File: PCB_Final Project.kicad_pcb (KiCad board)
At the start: 2 copper layers, 29 parts, among them J1 Conn_01x02_Socket, J2 Conn_01x02_Pin, J3 Conn_01x02_Socket, K1 Relay_SPDT, K2 Relay_SPDT, Q1 NPN, Q2 NPN, U1 WeMos_D1_mini, U2 PC817, U3 PC817

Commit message: small correction on pcb
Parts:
- moved REF** 10.8 mm to (134.6, 53.3)
- moved REF** 7.62 mm to (134.6, 121.9)
- moved REF** 7.62 mm to (33.0, 53.3)
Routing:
- net GND: track 270.7 -> 290.9 mm
- net Net-(D4-A): track 16.4 -> 13.6 mm
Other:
- board outline added: 114.3 x 81.3 mm
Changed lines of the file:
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@@
     (property "ki_keywords" "Single Pole Relay SPDT")
     (attr through_hole)
-    (fp_text reference "K1" (at 8.1 9.2) (layer "F.SilkS")
-        (effects (font (size 1 1) (thickness 0.15)))
-    )
-    (fp_text value "Relay_SPDT" (at 8 -9.6) (layer "F.Fab")
+    (fp_text reference "K1" (at 8.8152 -9.0368) (layer "F.SilkS")
+        (effects (font (size 1 1) (thickness 0.15)))
+    )
+    (fp_text value "Relay_SPDT" (at 8.3072 0.1072) (layer "F.Fab")
         (effects (font (size 1 1) (thickness 0.15)))
     )
@@
     (property "ki_keywords" "cap capacitor")
     (attr smd)
-    (fp_text reference "C1" (at 0 -1.68) (layer "F.SilkS")
+    (fp_text reference "C1" (at 0 1.778) (layer "F.SilkS")
         (effects (font (size 1 1) (thickness 0.15)))
     )
@@
     (property "ki_keywords" "R res resistor")
     (attr smd)
-    (fp_text reference "R3" (at 0 -1.65) (layer "F.SilkS")
+    (fp_text reference "R3" (at 0.6115 1.778) (layer "F.SilkS")
         (effects (font (size 1 1) (thickness 0.15)))
     )
@@
   )
   (footprint "MountingHole:MountingHole_3.2mm_M3" (layer "F.Cu")
-    (at 127 60.96)
+    (at 134.62 53.34)
     (descr "Mounting Hole 3.2mm, no annular, M3")
     (tags "mounting hole 3.2mm no annular m3")
@@
     (property "ki_keywords" "R res resistor")
     (attr smd)
-    (fp_text reference "R2" (at 0 -21.2598) (layer "F.SilkS")
+    (fp_text reference "R2" (at 0.0235 -1.7018) (layer "F.SilkS")
         (effects (font (size 1 1) (thickness 0.15)))
     )
@@
     (property "ki_keywords" "DHT22, temperature, humidity")
     (attr through_hole)
-    (fp_text reference "TH1" (at 0 7.35) (layer "F.SilkS")
+    (fp_text reference "TH1" (at 1.016 -4.318) (layer "F.SilkS")
         (effects (font (size 1 1) (thickness 0.15)))
     )
@@
     (property "ki_keywords" "connector")
     (attr exclude_from_pos_files)
-    (fp_text reference "J1" (at 4.4 -3.4 90) (layer "F.SilkS")
+    (fp_text reference "J1" (at 12.9286 0) (layer "F.SilkS")
         (effects (font (size 1 1) (thickness 0.15)))
     )
@@
     (property "ki_keywords" "LED diode")
     (attr smd)
-    (fp_text reference "POWER1" (at 0 -4.064) (layer "F.SilkS")
+    (fp_text reference "POWER1" (at 0 -1.778) (layer "F.SilkS")
         (effects (font (size 1 1) (thickness 0.15)))
     )
@@
   )
   (footprint "MountingHole:MountingHole_3.2mm_M3" (layer "F.Cu")
-    (at 33.02 60.96)
+    (at 33.02 53.34)
     (descr "Mounting Hole 3.2mm, no annular, M3")
     (tags "mounting hole 3.2mm no annular m3")
@@
   )
   (footprint "MountingHole:MountingHole_3.2mm_M3" (layer "F.Cu")
-    (at 127 121.92)
+    (at 134.62 121.92)
     (descr "Mounting Hole 3.2mm, no annular, M3")
     (tags "mounting hole 3.2mm no annular m3")
@@
     (property "ki_keywords" "connector")
     (attr exclude_from_pos_files)
-    (fp_text reference "J3" (at 4.4 -3.4 90) (layer "F.SilkS")
+    (fp_text reference "J3" (at 12.8016 -0.0508) (layer "F.SilkS")
         (effects (font (size 1 1) (thickness 0.15)))
     )
@@
     (property "ki_keywords" "LED diode")
     (attr smd)
-    (fp_text reference "D2" (at 0 -3.7846) (layer "F.SilkS")
+    (fp_text reference "D2" (at 1.1915 -1.7526) (layer "F.SilkS")
         (effects (font (size 1 1) (thickness 0.15)))
     )
@@
     (property "ki_keywords" "simulation")
     (attr smd)
-    (fp_text reference "Q1" (at 0 -2.45) (layer "F.SilkS")
+    (fp_text reference "Q1" (at 0 2.6924) (layer "F.SilkS")
         (effects (font (size 1 1) (thickness 0.15)))
     )
@@
     (property "ki_keywords" "NPN DC Optocoupler")
     (attr smd)
-    (fp_text reference "U3" (at 0 -3.6) (layer "F.SilkS")
+    (fp_text reference "U3" (at -1.0922 -3.556) (layer "F.SilkS")
         (effects (font (size 1 1) (thickness 0.15)))
     )
@@
     )
   )
+  (gr_rect (start 25.4 48.26) (end 139.7 129.54)
+    (stroke (width 0.1) (type default)) (fill none) (layer "Edge.Cuts"))
   (segment (start 64.77 87.63) (end 64.77 93.206) (width 0.33) (layer "F.Cu") (net 1))
   (segment (start 62.23 87.63) (end 62.23 93.206) (width 0.33) (layer "F.Cu") (net 2))
   (segment (start 48.163 54.864) (end 48.163 58.577) (width 1) (layer "F.Cu") (net 3))
+  (segment (start 101.5638 100.6898) (end 99.3074 102.9462) (width 1) (layer "F.Cu") (net 3))
+  (segment (start 101.5638 99.3648) (end 101.5638 100.6898) (width 1) (layer "F.Cu") (net 3))
   (segment (start 57.15 93.206) (end 54.852 93.206) (width 1) (layer "F.Cu") (net 3))
   (segment (start 54.852 93.206) (end 49.53 87.884) (width 1) (layer "F.Cu") (net 3))
@@
   (segment (start 84.9376 89.3064) (end 86.2076 89.3064) (width 1) (layer "F.Cu") (net 3))
   (segment (start 87.0204 90.1192) (end 87.0204 99.568) (width 1) (layer "F.Cu") (net 3))
+  (segment (start 99.3074 102.9462) (end 83.6422 102.9462) (width 1) (layer "F.Cu") (net 3))
   (segment (start 93.9038 66.294) (end 95.1992 67.5894) (width 1) (layer "F.Cu") (net 3))
   (segment (start 95.1992 67.5894) (end 95.1992 69.7992) (width 1) (layer "F.Cu") (net 3))
@@
   (segment (start 81.0906 82.3468) (end 85.2424 78.195) (width 0.33) (layer "F.Cu") (net 16))
   (segment (start 85.2424 78.195) (end 85.2424 74.6506) (width 0.33) (layer "F.Cu") (net 16))
-  (segment (start 98.9438 98.4148) (end 101.1384 100.6094) (width 0.33) (layer "F.Cu") (net 22))
-  (segment (start 95.3662 97.322) (end 96.4946 98.4504) (width 0.33) (layer "F.Cu") (net 22))
-  (segment (start 95.3662 95.7072) (end 95.3662 97.322) (width 0.33) (layer "F.Cu") (net 22))
-  (segment (start 101.1384 100.6094) (end 105.425 100.6094) (width 0.33) (layer "F.Cu") (net 22))
-  (segment (start 96.5302 98.4148) (end 98.9438 98.4148) (width 0.33) (layer "F.Cu") (net 22))
-  (segment (start 96.4946 98.4504) (end 96.5302 98.4148) (width 0.33) (layer "F.Cu") (net 22))
-  (segment (start 105.425 100.6094) (end 107.7928 98.2416) (width 0.33) (layer "F.Cu") (net 22))
+  (segment (start 107.6196 98.4148) (end 107.7928 98.2416) (width 0.33) (layer "F.Cu") (net 22))
+  (segment (start 98.0738 98.4148) (end 98.9438 98.4148) (width 0.33) (layer "F.Cu") (net 22))
+  (segment (start 95.3662 95.7072) (end 98.0738 98.4148) (width 0.33) (layer "F.Cu") (net 22))
+  (segment (start 98.9438 98.4148) (end 107.6196 98.4148) (width 0.33) (layer "F.Cu") (net 22))
   (segment (start 131.064 110.2106) (end 120.0238 110.2106) (width 2) (layer "F.Cu") (net 23))
   (segment (start 116.8146 107.0634) (end 116.8146 92.583) (width 2) (layer "F.Cu") (net 23))

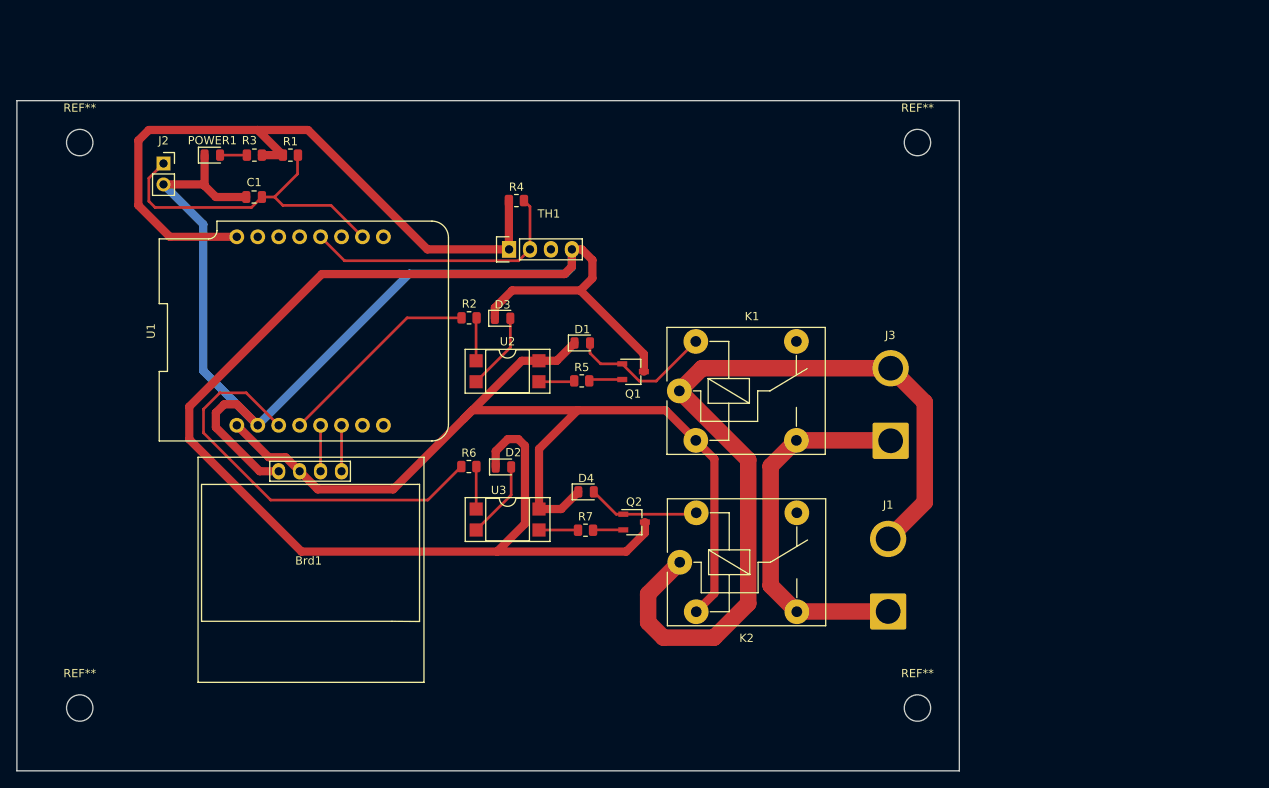
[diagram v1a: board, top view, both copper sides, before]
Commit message: add alternate power & revamp pcb
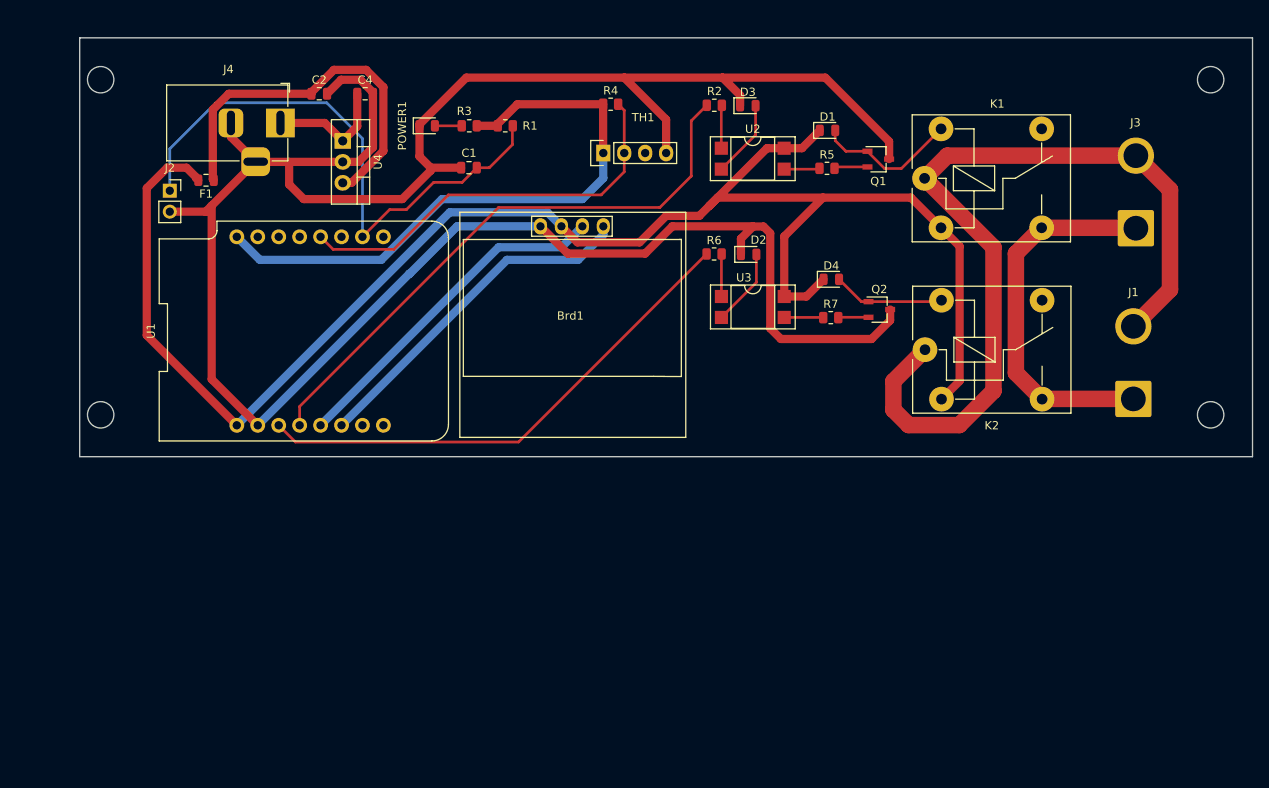
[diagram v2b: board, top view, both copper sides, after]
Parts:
- added C2: 0.33uF, Capacitor_SMD:C_0805_2012Metric, F.Cu at (62.1, 47.4)
- added C4: 0.33uF, Capacitor_SMD:C_0805_2012Metric, F.Cu at (67.6, 47.4)
- added F1: Fuse, Fuse:Fuse_0805_2012Metric, F.Cu at (48.3, 57.9)
- added J4: Barrel_Jack_Switch, Connector_BarrelJack:BarrelJack_Horizontal, F.Cu at (57.4, 51.0)
- added U4: LM7805_TO220, Package_TO_SOT_THT:TO-220-3_Vertical, F.Cu at (64.9, 53.1)
- moved REF** 50.3 mm to (170.2, 86.4)
- moved Brd1 43.5 mm to (92.5, 74.1)
- moved D1 39.4 mm to (123.7, 51.9)
- moved D2 39.4 mm to (114.1, 66.9)
- moved J1 39.4 mm to (160.8, 84.4)
- moved J3 39.4 mm to (161.1, 63.7)
- moved K2 39.4 mm to (135.5, 78.5)
- moved R7 39.4 mm to (124.1, 74.6)
- moved U2 39.4 mm to (114.6, 55.3)
- moved U3 39.4 mm to (114.7, 73.3)
- moved D4 39.4 mm to (124.2, 69.9)
- moved K1 39.4 mm to (135.5, 57.7)
- moved Q1 39.4 mm to (129.9, 55.3)
- moved Q2 39.4 mm to (130.0, 73.6)
- moved R2 39.4 mm to (110.0, 48.8)
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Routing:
- net /5V: track 123.7 -> 202.0 mm
- net Net-(U4-VO): track 0.00 -> 46.6 mm
- net /IN: track 25.0 -> 70.7 mm
- net /SDA: track 5.58 -> 42.3 mm
- net /SCL: track 5.58 -> 41.7 mm
- net /ANALOG_MOISTURE: track 40.3 -> 69.6 mm
- net /DHT_DATA: track 33.4 -> 49.9 mm
- net Net-(U4-VI): track 0.00 -> 14.9 mm
- net /IN2: track 50.8 -> 62.2 mm
- net /3.3V: track 85.6 -> 75.2 mm
- net GND: track 290.9 -> 296.6 mm
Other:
- board size 114.3 x 81.3 mm -> 142.2 x 50.8 mm

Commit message: final commit
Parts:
- 5V - 24V: renamed from J4
- WeMos D1 Mini: renamed from U1
- moved REF** 3.59 mm to (38.1, 88.9)
- moved REF** 3.59 mm to (38.1, 43.2)
- moved REF** 2.54 mm to (170.2, 88.9)
- moved REF** 2.54 mm to (170.2, 43.2)
- renumbered D3 to 1, D2 to 2, F1 to FUSE, J2 to MOISTURE, Brd1 to OLED, J3 to RELAY1, J1 to RELAY2
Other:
- board size 142.2 x 50.8 mm -> 142.2 x 55.9 mm
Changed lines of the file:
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@@
   )
   (footprint "MountingHole:MountingHole_3.2mm_M3" (layer "F.Cu")
-    (at 170.18 45.72)
+    (at 170.18 43.18)
     (descr "Mounting Hole 3.2mm, no annular, M3")
     (tags "mounting hole 3.2mm no annular m3")
@@
         (effects (font (size 1 1) (thickness 0.15)))
     )
-    (fp_text value "DHT22_Temperature_Humidity" (at 0 -14.1648) (layer "F.Fab")
+    (fp_text value "DHT22_Temperature_Humidity" (at 0 -11.43) (layer "F.Fab")
         (effects (font (size 1 1) (thickness 0.15)))
     )
@@
     (property "ki_keywords" "NPN DC Optocoupler")
     (attr smd)
-    (fp_text reference "U2" (at 0 -3.6) (layer "F.SilkS")
+    (fp_text reference "U2" (at -1.487 -3.6068) (layer "F.SilkS")
         (effects (font (size 1 1) (thickness 0.15)))
     )
@@
     (property "ki_keywords" "connector")
     (attr exclude_from_pos_files)
-    (fp_text reference "J1" (at 12.9286 0) (layer "F.SilkS")
+    (fp_text reference "RELAY2" (at 12.9286 -0.7874) (layer "F.SilkS")
         (effects (font (size 1 1) (thickness 0.15)))
     )
@@
     (property "ki_keywords" "esp8266, wemos")
     (attr through_hole)
-    (fp_text reference "U1" (at -19.3 0 90) (layer "F.SilkS")
-        (effects (font (size 1 1) (thickness 0.15)))
-    )
-    (fp_text value "WeMos_D1_mini" (at 0 0) (layer "F.Fab")
+    (fp_text reference "WeMos D1 Mini" (at -4.3688 -0.0762 180) (layer "F.SilkS")
+        (effects (font (size 1 1) (thickness 0.15)))
+    )
+    (fp_text value "WeMos_D1_mini" (at 8.509 7.9502) (layer "F.Fab")
         (effects (font (size 1 1) (thickness 0.15)))
     )
@@
     (property "ki_keywords" "LED diode")
     (attr smd)
-    (fp_text reference "D3" (at 0 -1.65) (layer "F.SilkS")
+    (fp_text reference "1" (at 0.5819 -1.7272) (layer "F.SilkS")
         (effects (font (size 1 1) (thickness 0.15)))
     )
@@
   )
   (footprint "MountingHole:MountingHole_3.2mm_M3" (layer "F.Cu")
-    (at 35.56 86.36)
+    (at 38.1 88.9)
     (descr "Mounting Hole 3.2mm, no annular, M3")
     (tags "mounting hole 3.2mm no annular m3")
@@
   )
   (footprint "MountingHole:MountingHole_3.2mm_M3" (layer "F.Cu")
-    (at 35.56 45.72)
+    (at 38.1 43.18)
     (descr "Mounting Hole 3.2mm, no annular, M3")
     (tags "mounting hole 3.2mm no annular m3")
@@
         (effects (font (size 1 1) (thickness 0.15)))
     )
-    (fp_text value "MountingHole_3.2mm_M3" (at -1.4224 6.4516) (layer "F.Fab")
+    (fp_text value "MountingHole_3.2mm_M3" (at -1.4224 5.08) (layer "F.Fab")
         (effects (font (size 1 1) (thickness 0.15)))
     )
@@
   )
   (footprint "MountingHole:MountingHole_3.2mm_M3" (layer "F.Cu")
-    (at 170.18 86.36)
+    (at 170.18 88.9)
     (descr "Mounting Hole 3.2mm, no annular, M3")
     (tags "mounting hole 3.2mm no annular m3")
@@
     (property "ki_keywords" "SSD1306")
     (attr through_hole)
-    (fp_text reference "Brd1" (at 0 0.254) (layer "F.SilkS")
+    (fp_text reference "OLED" (at 0 0.254) (layer "F.SilkS")
         (effects (font (size 1 1) (thickness 0.15)))
     )
@@
     (property "ki_keywords" "DC power barrel jack connector")
     (attr through_hole)
-    (fp_text reference "J4" (at -6.3048 -6.5101) (layer "F.SilkS")
+    (fp_text reference "5V - 24V" (at -6.3048 -6.8403) (layer "F.SilkS")
         (effects (font (size 1 1) (thickness 0.15)))
     )
@@
     (property "ki_keywords" "fuse")
     (attr smd)
-    (fp_text reference "F1" (at 0 -1.65) (layer "F.SilkS")
-        (effects (font (size 1 1) (thickness 0.15)))
+    (fp_text reference "FUSE" (at 0.7643 -1.7272) (layer "F.SilkS")
+        (effects (font (size 0.8 0.8) (thickness 0.15)))
     )
     (fp_text value "Fuse" (at 0 1.65) (layer "F.Fab")
@@
     (property "ki_keywords" "connector")
     (attr exclude_from_pos_files)
-    (fp_text reference "J3" (at 12.8016 -0.0508) (layer "F.SilkS")
+    (fp_text reference "RELAY1" (at 12.8016 -1.0922) (layer "F.SilkS")
         (effects (font (size 1 1) (thickness 0.15)))
     )
@@
     (property "ki_keywords" "LED diode")
     (attr smd)
-    (fp_text reference "D2" (at 1.1915 -1.7526) (layer "F.SilkS")
+    (fp_text reference "2" (at 1.1153 -1.7526) (layer "F.SilkS")
         (effects (font (size 1 1) (thickness 0.15)))
     )
@@
     (property "ki_keywords" "NPN DC Optocoupler")
     (attr smd)
-    (fp_text reference "U3" (at -1.0922 -3.556) (layer "F.SilkS")
+    (fp_text reference "U3" (at -1.7526 -3.5814) (layer "F.SilkS")
         (effects (font (size 1 1) (thickness 0.15)))
     )
@@
     (property "ki_keywords" "connector")
     (attr through_hole)
-    (fp_text reference "J2" (at 0 -2.77) (layer "F.SilkS")
-        (effects (font (size 1 1) (thickness 0.15)))
+    (fp_text reference "MOISTURE" (at 0.9906 5.0292) (layer "F.SilkS")
+        (effects (font (size 0.8 0.8) (thickness 0.15)))
     )
     (fp_text value "Conn_01x02_Pin" (at -5.08 -5.08) (layer "F.Fab")
@@
     )
   )
-  (gr_rect (start 33.02 40.64) (end 175.26 91.44)
+  (gr_rect (start 33.02 38.1) (end 175.26 93.98)
     (stroke (width 0.1) (type default)) (fill none) (layer "Edge.Cuts"))
   (segment (start 64.77 87.63) (end 84.836 67.564) (width 1) (layer "B.Cu") (net 1))
@@
   (segment (start 57.3588 50.9601) (end 62.7328 50.9601) (width 1) (layer "F.Cu") (net 33))
   (segment (start 61.1174 47.253297) (end 63.850697 44.52) (width 1) (layer "F.Cu") (net 34))
-  (segment (start 64.9757 58.166) (end 64.9172 58.2245) (width 1) (layer "F.Cu") (net 34))
   (segment (start 69.85 54.353756) (end 65.979256 58.2245) (width 1) (layer "F.Cu") (net 34))
   (segment (start 63.850697 44.52) (end 67.746703 44.52) (width 1) (layer "F.Cu") (net 34))
